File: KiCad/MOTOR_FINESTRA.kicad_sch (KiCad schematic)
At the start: 0 parts

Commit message: Actulització del driver del motor de finestra
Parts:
- added C10: 10uF, symbol Device:C
- added C11, C12, C9: 100nF, symbol Device:C
- added U3: VNH5019A-E, Package_SO:ST_MultiPowerSO-30, symbol Driver_Motor:VNH5019A-E
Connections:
- new net: C12.2, U3.11 (CP)
- new net GND: C10.2, C11.2, C12.1, C9.2, U3.6 (CS_DIS)
- new net GND_PWR: U3.18 (GNDB), U3.19 (GNDB), U3.20 (GNDB), U3.26 (GNDA), U3.27 (GNDA), U3.28 (GNDA)
- new net VBAT_PROT: C10.1, C9.1, U3.12 (VBAT)
- new net VDD_3V3: C11.1, U3.13 (VCC), U3.23 (VCC), U3.3 (VCC), U3.31 (VCC)
- new net WIN_CURRENT_ADC: U3.8 (CS)
- new net WIN_DIAGA: U3.5 (EN/DIAGA)
- new net WIN_DIAGB: U3.9 (EN/DIAGB)
- new net WIN_INA: U3.4 (INA)
- new net WIN_INB: U3.10 (INB)
- new net WIN_MOTOR_A: U3.1 (OUTA), U3.25 (OUTA), U3.30 (OUTA), U3.33 (OUTA)
- new net WIN_MOTOR_B: U3.15 (OUTB), U3.16 (OUTB), U3.21 (OUTB), U3.32 (OUTB)
- new net WIN_PWM: U3.7 (PWM)

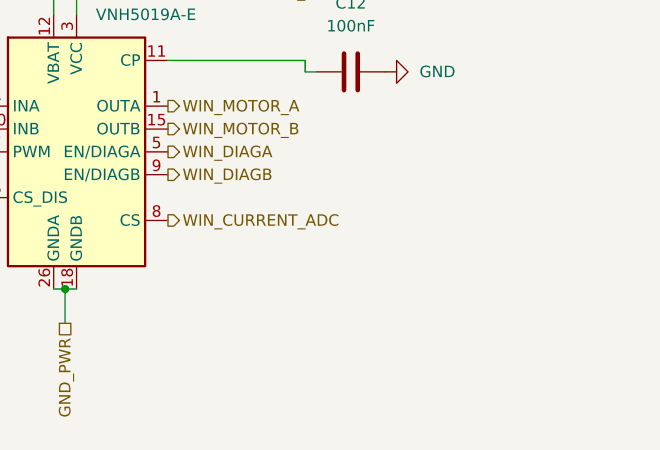
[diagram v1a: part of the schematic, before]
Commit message: Esquematic general conectat
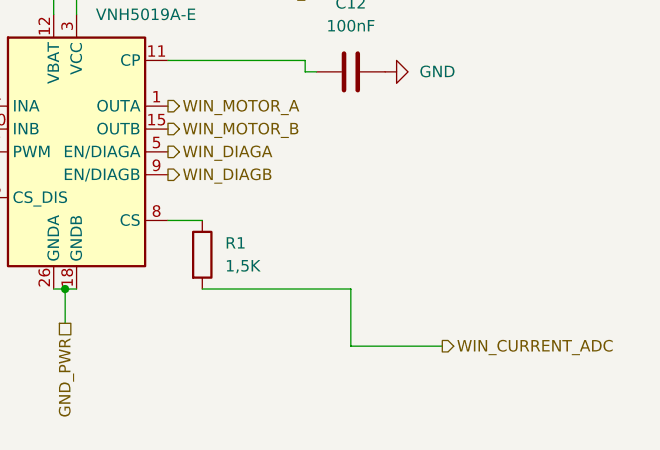
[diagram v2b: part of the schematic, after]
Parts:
- added R1: 1,5K, symbol Device:R
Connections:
- net WIN_CURRENT_ADC: now also R1.2; no longer U3.8 (CS)
- new net: R1.1, U3.8 (CS)
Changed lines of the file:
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@@
+	(wire
+		(pts
+			(xy 162.56 106.68) (xy 146.05 106.68)
+		)
+		(stroke
+			(width 0)
+			(type default)
+		)
+	)
+	(wire
+		(pts
+			(xy 162.56 106.68) (xy 162.56 113.03)
+		)
+		(stroke
+			(width 0)
+			(type default)
+		)
+	)
+	(wire
+		(pts
+			(xy 162.56 113.03) (xy 172.72 113.03)
+		)
+		(stroke
+			(width 0)
+			(type default)
+		)
+	)
+	(wire
+		(pts
+			(xy 142.24 99.06) (xy 146.05 99.06)
+		)
+		(stroke
+			(width 0)
+			(type default)
+		)
+	)
 	(wire
 		(pts
@@
 	(hierarchical_label "WIN_CURRENT_ADC"
 		(shape output)
-		(at 142.24 99.06 0)
+		(at 172.72 113.03 0)
 		(effects
 			(font
@@
 					(unit 1)
 				)
+			)
+		)
+	)
+	(symbol
+		(lib_id "Device:R")
+		(at 146.05 102.87 0)
+		(unit 1)
+		(exclude_from_sim no)
+		(in_bom yes)
+		(on_board yes)
+		(dnp no)
+		(fields_autoplaced yes)
+		(property "Reference" "R1"
+			(at 148.59 101.5999 0)
+			(effects
+				(font
+					(size 1.27 1.27)
+				)
+				(justify left)
+			)
+		)
+		(property "Value" "1,5K"
+			(at 148.59 104.1399 0)
+			(effects
+				(font
+					(size 1.27 1.27)
+				)
+				(justify left)
+			)
+		)
+		(property "Footprint" ""
+			(at 144.272 102.87 90)
+			(effects
+				(font
+					(size 1.27 1.27)
+				)
+				(hide yes)
+			)
+		)
+		(property "Datasheet" "~"
+			(at 146.05 102.87 0)
+			(effects
+				(font
+					(size 1.27 1.27)
+				)
+				(hide yes)
+			)
+		)
+		(property "Description" "Resistor"
+			(at 146.05 102.87 0)
+			(effects
+				(font
+					(size 1.27 1.27)
+				)
+				(hide yes)
+			)
+		)
+		(pin "2"
+		)
+		(pin "1"
+		)
+		(instances
+			(project ""
+				(path "/347831db-5db9-4aff-ad32-e56fd770e219/b6effc59-48f1-49a7-95ce-6407716902cc"
+					(reference "R1")
+					(unit 1)
+				)

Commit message: ESQUEMATIC FINAL V.1
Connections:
- net GND: now also R1.2
- net WIN_CURRENT_ADC: now also R1.1, U3.8 (CS); no longer R1.2
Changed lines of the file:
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@@
 	(paper "A4")
+	(junction
+		(at 146.05 99.06)
+		(diameter 0)
+		(color 0 0 0 0)
+	)
 	(junction
 		(at 129.54 69.85)
@@
 	(wire
 		(pts
-			(xy 162.56 106.68) (xy 146.05 106.68)
-		)
-		(stroke
-			(width 0)
-			(type default)
-		)
-	)
-	(wire
-		(pts
-			(xy 162.56 106.68) (xy 162.56 113.03)
-		)
-		(stroke
-			(width 0)
-			(type default)
-		)
-	)
-	(wire
-		(pts
-			(xy 162.56 113.03) (xy 172.72 113.03)
+			(xy 149.86 99.06) (xy 146.05 99.06)
 		)
 		(stroke
@@
 	(hierarchical_label "WIN_CURRENT_ADC"
 		(shape output)
-		(at 172.72 113.03 0)
+		(at 149.86 99.06 0)
 		(effects
 			(font
@@
 					(unit 1)
 				)
+			)
+		)
+	)
+	(symbol
+		(lib_id "power:GND")
+		(at 146.05 106.68 0)
+		(unit 1)
+		(exclude_from_sim no)
+		(in_bom yes)
+		(on_board yes)
+		(dnp no)
+		(fields_autoplaced yes)
+		(property "Reference" "#PWR08"
+			(at 146.05 113.03 0)
+			(effects
+				(font
+					(size 1.27 1.27)
+				)
+				(hide yes)
+			)
+		)
+		(property "Value" "GND"
+			(at 146.05 111.76 0)
+			(effects
+				(font
+					(size 1.27 1.27)
+				)
+			)
+		)
+		(property "Footprint" ""
+			(at 146.05 106.68 0)
+			(effects
+				(font
+					(size 1.27 1.27)
+				)
+				(hide yes)
+			)
+		)
+		(property "Datasheet" ""
+			(at 146.05 106.68 0)
+			(effects
+				(font
+					(size 1.27 1.27)
+				)
+				(hide yes)
+			)
+		)
+		(property "Description" "Power symbol creates a global label with name \"GND\" , ground"
+			(at 146.05 106.68 0)
+			(effects
+				(font
+					(size 1.27 1.27)
+				)
+				(hide yes)
+			)
+		)
+		(pin "1"
+		)
+		(instances
+			(project "PROJECTE_EINES"
+				(path "/347831db-5db9-4aff-ad32-e56fd770e219/b6effc59-48f1-49a7-95ce-6407716902cc"
+					(reference "#PWR08")
+					(unit 1)
+				)

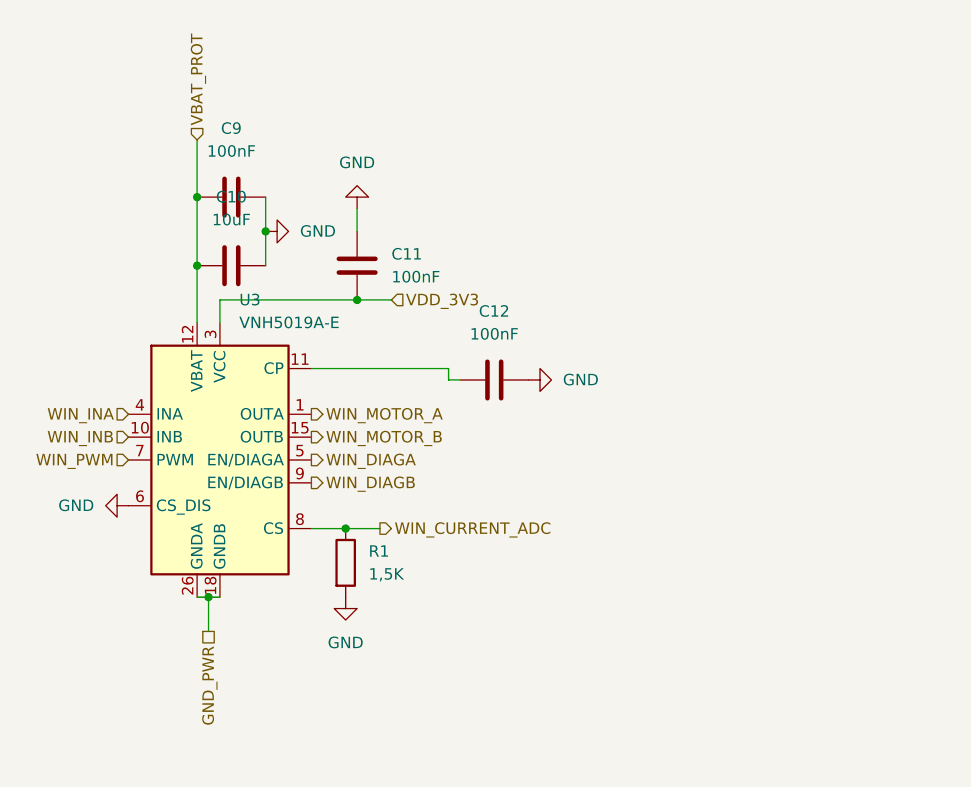
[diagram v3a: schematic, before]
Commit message: Nova versió diagrama de blocs + BOM actualitzat + Nova versió KiCad
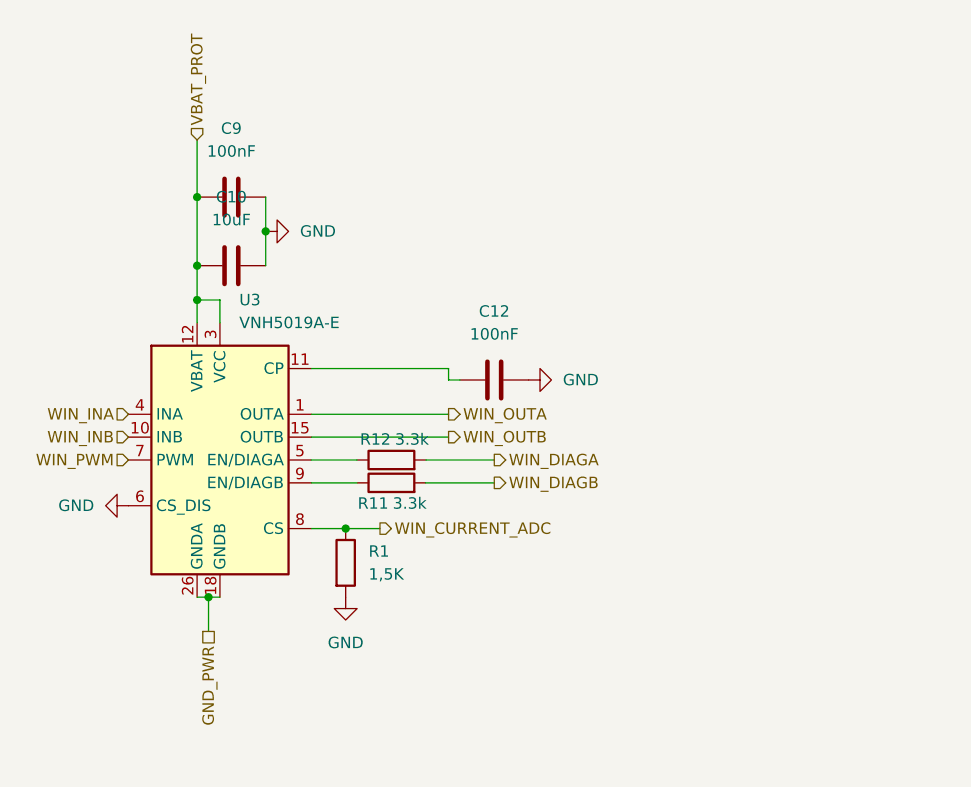
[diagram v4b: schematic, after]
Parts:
- removed C11: 100nF, symbol Device:C
- added R11, R12: 3.3k, Resistor_SMD:R_0805_2012Metric_Pad1.20x1.40mm_HandSolder, symbol Device:R
- R1: footprint (none) -> Resistor_SMD:R_0805_2012Metric_Pad1.20x1.40mm_HandSolder
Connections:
- net VDD_3V3 is gone; now on net VBAT_PROT: U3.13 (VCC), U3.23 (VCC), U3.3 (VCC), U3.31 (VCC)
- net WIN_DIAGA: now also R12.2; no longer U3.5 (EN/DIAGA)
- net WIN_DIAGB: now also R11.2; no longer U3.9 (EN/DIAGB)
- net WIN_MOTOR_A renamed WIN_OUTA
- net WIN_MOTOR_B renamed WIN_OUTB
- new net: R12.1, U3.5 (EN/DIAGA)
- new net: R11.1, U3.9 (EN/DIAGB)

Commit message: Resistències pull-up arreglades als motors
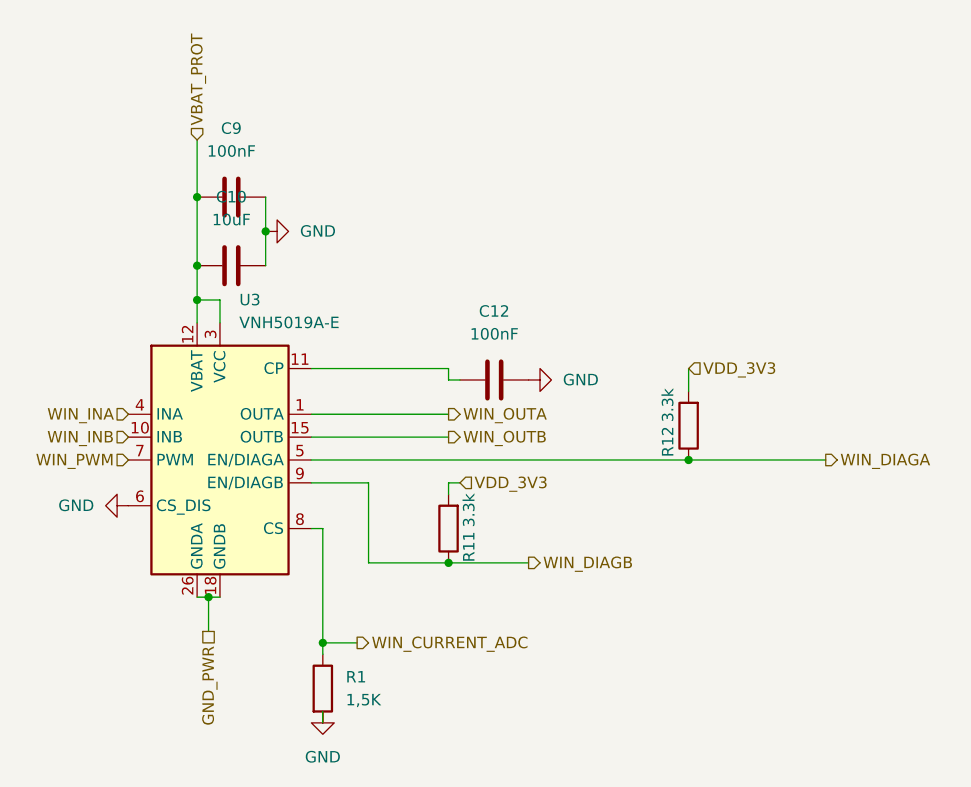
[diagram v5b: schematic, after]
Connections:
- net WIN_DIAGA: now also R12.1, U3.5 (EN/DIAGA); no longer R12.2
- net WIN_DIAGB: now also R11.1, U3.9 (EN/DIAGB); no longer R11.2
- new net VDD_3V3: R11.2, R12.2
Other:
- moved on the sheet: R1, R11, R12
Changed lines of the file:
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@@
 	)
 	(junction
-		(at 146.05 99.06)
+		(at 157.48 102.87)
+		(diameter 0)
+		(color 0 0 0 0)
+	)
+	(junction
+		(at 143.51 111.76)
 		(diameter 0)
 		(color 0 0 0 0)
@@
 	)
 	(junction
+		(at 184.15 91.44)
+		(diameter 0)
+		(color 0 0 0 0)
+	)
+	(junction
 		(at 129.54 62.23)
 		(diameter 0)
@@
 	(wire
 		(pts
-			(xy 147.32 93.98) (xy 142.24 93.98)
-		)
-		(stroke
-			(width 0)
-			(type default)
-		)
-	)
-	(wire
-		(pts
-			(xy 147.32 91.44) (xy 142.24 91.44)
-		)
-		(stroke
-			(width 0)
-			(type default)
-		)
-	)
-	(wire
-		(pts
-			(xy 162.56 93.98) (xy 154.94 93.98)
+			(xy 148.59 102.87) (xy 157.48 102.87)
+		)
+		(stroke
+			(width 0)
+			(type default)
+		)
+	)
+	(wire
+		(pts
+			(xy 142.24 91.44) (xy 184.15 91.44)
+		)
+		(stroke
+			(width 0)
+			(type default)
+		)
+	)
+	(wire
+		(pts
+			(xy 158.75 93.98) (xy 157.48 93.98)
 		)
 		(stroke
@@
 	(wire
 		(pts
+			(xy 148.59 102.87) (xy 148.59 93.98)
+		)
+		(stroke
+			(width 0)
+			(type default)
+		)
+	)
+	(wire
+		(pts
 			(xy 130.81 106.68) (xy 130.81 110.49)
 		)
@@
 	(wire
 		(pts
-			(xy 149.86 99.06) (xy 146.05 99.06)
-		)
-		(stroke
-			(width 0)
-			(type default)
-		)
-	)
-	(wire
-		(pts
-			(xy 142.24 99.06) (xy 146.05 99.06)
+			(xy 147.32 111.76) (xy 143.51 111.76)
 		)
 		(stroke
@@
 	(wire
 		(pts
+			(xy 148.59 93.98) (xy 142.24 93.98)
+		)
+		(stroke
+			(width 0)
+			(type default)
+		)
+	)
+	(wire
+		(pts
 			(xy 129.54 73.66) (xy 132.08 73.66)
 		)
@@
 	(wire
 		(pts
+			(xy 157.48 93.98) (xy 157.48 95.25)
+		)
+		(stroke
+			(width 0)
+			(type default)
+		)
+	)
+	(wire
+		(pts
 			(xy 129.54 69.85) (xy 129.54 73.66)
 		)
@@
 	(wire
 		(pts
+			(xy 143.51 111.76) (xy 143.51 99.06)
+		)
+		(stroke
+			(width 0)
+			(type default)
+		)
+	)
+	(wire
+		(pts
+			(xy 184.15 81.28) (xy 184.15 83.82)
+		)
+		(stroke
+			(width 0)
+			(type default)
+		)
+	)
+	(wire
+		(pts
 			(xy 157.48 82.55) (xy 158.75 82.55)
 		)
@@
 	(wire
 		(pts
-			(xy 162.56 91.44) (xy 154.94 91.44)
-		)
-		(stroke
-			(width 0)
-			(type default)
-		)
-	)
-	(wire
-		(pts
 			(xy 129.54 62.23) (xy 129.54 69.85)
 		)
@@
 	(wire
 		(pts
+			(xy 157.48 102.87) (xy 166.37 102.87)
+		)
+		(stroke
+			(width 0)
+			(type default)
+		)
+	)
+	(wire
+		(pts
 			(xy 142.24 86.36) (xy 157.48 86.36)
 		)
@@
 	(wire
 		(pts
+			(xy 143.51 120.65) (xy 143.51 119.38)
+		)
+		(stroke
+			(width 0)
+			(type default)
+		)
+	)
+	(wire
+		(pts
 			(xy 157.48 81.28) (xy 142.24 81.28)
 		)
@@
 			(width 0)
 			(type default)
+		)
+	)
+	(wire
+		(pts
+			(xy 143.51 99.06) (xy 142.24 99.06)
+		)
+		(stroke
+			(width 0)
+			(type default)
+		)
+	)
+	(wire
+		(pts
+			(xy 184.15 91.44) (xy 199.39 91.44)
+		)
+		(stroke
+			(width 0)
+			(type default)
+		)
+	)
+	(wire
+		(pts
+			(xy 143.51 113.03) (xy 143.51 111.76)
+		)
+		(stroke
+			(width 0)
+			(type default)
+		)
+	)
+	(hierarchical_label "VDD_3V3"
+		(shape input)
+		(at 158.75 93.98 0)
+		(effects
+			(font
+				(size 1.27 1.27)
+			)
+			(justify left)
+		)
+	)
+	(hierarchical_label "VDD_3V3"
+		(shape input)
+		(at 184.15 81.28 0)
+		(effects
+			(font
+				(size 1.27 1.27)
+			)
+			(justify left)
 		)
 	)
@@
 	(hierarchical_label "WIN_DIAGA"
 		(shape output)
-		(at 162.56 91.44 0)
+		(at 199.39 91.44 0)
 		(effects
 			(font
@@
 	(hierarchical_label "WIN_CURRENT_ADC"
 		(shape output)
-		(at 149.86 99.06 0)
+		(at 147.32 111.76 0)
 		(effects
 			(font
@@
 	(hierarchical_label "WIN_DIAGB"
 		(shape output)
-		(at 162.56 93.98 0)
+		(at 166.37 102.87 0)
 		(effects
 			(font
@@
 	(symbol
 		(lib_id "Device:R")
-		(at 151.13 91.44 90)
+		(at 184.15 87.63 180)
 		(unit 1)
 		(exclude_from_sim no)
@@
 		(dnp no)
 		(property "Reference" "R12"
-			(at 149.352 89.154 90)
+			(at 181.864 89.408 90)
 			(effects
 				(font
@@
 		)
 		(property "Value" "3.3k"
-			(at 153.416 89.154 90)
+			(at 181.864 85.344 90)
 			(effects
 				(font
@@
 		)
 		(property "Footprint" "Resistor_SMD:R_0805_2012Metric_Pad1.20x1.40mm_HandSolder"
-			(at 151.13 93.218 90)
+			(at 185.928 87.63 90)
 			(effects
 				(font
@@
 		)
 		(property "Datasheet" "~"
-			(at 151.13 91.44 0)
+			(at 184.15 87.63 0)
 			(effects
 				(font
@@
 		)
 		(property "Description" "Resistor"
-			(at 151.13 91.44 0)
+			(at 184.15 87.63 0)
 			(effects
 				(font
@@
 	(symbol
 		(lib_id "Device:R")
-		(at 151.13 93.98 90)
+		(at 157.48 99.06 180)
 		(unit 1)
 		(exclude_from_sim no)
@@
 		(dnp no)
 		(property "Reference" "R11"
-			(at 149.098 96.266 90)
+			(at 159.766 101.092 90)
 			(effects
 				(font
@@
 		)
 		(property "Value" "3.3k"
-			(at 153.162 96.266 90)
+			(at 159.766 97.028 90)
 			(effects
 				(font
@@
 		)
 		(property "Footprint" "Resistor_SMD:R_0805_2012Metric_Pad1.20x1.40mm_HandSolder"
-			(at 151.13 95.758 90)
+			(at 159.258 99.06 90)
 			(effects
 				(font
@@
 		)
 		(property "Datasheet" "~"
-			(at 151.13 93.98 0)
+			(at 157.48 99.06 0)
 			(effects
 				(font
@@
 		)
 		(property "Description" "Resistor"
-			(at 151.13 93.98 0)
+			(at 157.48 99.06 0)
 			(effects
 				(font
@@
 	(symbol
 		(lib_id "power:GND")
-		(at 146.05 106.68 0)
+		(at 143.51 119.38 0)
 		(unit 1)
 		(exclude_from_sim no)
@@
 		(fields_autoplaced yes)
 		(property "Reference" "#PWR08"
-			(at 146.05 113.03 0)
+			(at 143.51 125.73 0)
 			(effects
 				(font
@@
 		)
 		(property "Value" "GND"
-			(at 146.05 111.76 0)
+			(at 143.51 124.46 0)
 			(effects
 				(font
@@
 		)
 		(property "Footprint" ""
-			(at 146.05 106.68 0)
+			(at 143.51 119.38 0)
 			(effects
 				(font
@@
 		)
 		(property "Datasheet" ""
-			(at 146.05 106.68 0)
+			(at 143.51 119.38 0)
 			(effects
 				(font
@@
 		)
 		(property "Description" "Power symbol creates a global label with name \"GND\" , ground"
-			(at 146.05 106.68 0)
+			(at 143.51 119.38 0)
 			(effects
 				(font
@@
 	(symbol
 		(lib_id "Device:R")
-		(at 146.05 102.87 0)
+		(at 143.51 116.84 0)
 		(unit 1)
 		(exclude_from_sim no)
@@
 		(fields_autoplaced yes)
 		(property "Reference" "R1"
-			(at 148.59 101.5999 0)
+			(at 146.05 115.5699 0)
 			(effects
 				(font
@@
 		)
 		(property "Value" "1,5K"
-			(at 148.59 104.1399 0)
+			(at 146.05 118.1099 0)
 			(effects
 				(font
@@
 		)
 		(property "Footprint" "Resistor_SMD:R_0805_2012Metric_Pad1.20x1.40mm_HandSolder"
-			(at 144.272 102.87 90)
+			(at 141.732 116.84 90)
 			(effects
 				(font
@@
 		)
 		(property "Datasheet" "~"
-			(at 146.05 102.87 0)
+			(at 143.51 116.84 0)
 			(effects
 				(font
@@
 		)
 		(property "Description" "Resistor"
-			(at 146.05 102.87 0)
-			(effects
-				(font
+			(at 143.51 116.84 0)
+			(effects
+				(font

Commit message: Etiquetes de GND i VCC 3.3V canviades a simbols
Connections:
- net GND_PWR renamed GNDPWR
- net VDD_3V3 renamed +3.3V
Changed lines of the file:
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@@
-	(wire
-		(pts
-			(xy 158.75 93.98) (xy 157.48 93.98)
-		)
-		(stroke
-			(width 0)
-			(type default)
-		)
-	)
 	(wire
 		(pts
@@
 	(wire
 		(pts
-			(xy 157.48 93.98) (xy 157.48 95.25)
-		)
-		(stroke
-			(width 0)
-			(type default)
-		)
-	)
-	(wire
-		(pts
 			(xy 129.54 69.85) (xy 129.54 73.66)
 		)
@@
 			(width 0)
 			(type default)
-		)
-	)
-	(hierarchical_label "VDD_3V3"
-		(shape input)
-		(at 158.75 93.98 0)
-		(effects
-			(font
-				(size 1.27 1.27)
-			)
-			(justify left)
-		)
-	)
-	(hierarchical_label "VDD_3V3"
-		(shape input)
-		(at 184.15 81.28 0)
-		(effects
-			(font
-				(size 1.27 1.27)
-			)
-			(justify left)
 		)
 	)
@@
 		)
 	)
-	(hierarchical_label "GND_PWR"
-		(shape passive)
-		(at 130.81 110.49 270)
-		(effects
-			(font
-				(size 1.27 1.27)
-			)
-			(justify right)
-		)
-	)
 	(hierarchical_label "WIN_OUTB"
 		(shape output)
@@
 			)
 			(justify left)
+		)
+	)
+	(symbol
+		(lib_id "power:GNDPWR")
+		(at 130.81 110.49 0)
+		(unit 1)
+		(exclude_from_sim no)
+		(in_bom yes)
+		(on_board yes)
+		(dnp no)
+		(fields_autoplaced yes)
+		(property "Reference" "#PWR037"
+			(at 130.81 115.57 0)
+			(effects
+				(font
+					(size 1.27 1.27)
+				)
+				(hide yes)
+			)
+		)
+		(property "Value" "GNDPWR"
+			(at 130.683 114.3 0)
+			(effects
+				(font
+					(size 1.27 1.27)
+				)
+			)
+		)
+		(property "Footprint" ""
+			(at 130.81 111.76 0)
+			(effects
+				(font
+					(size 1.27 1.27)
+				)
+				(hide yes)
+			)
+		)
+		(property "Datasheet" ""
+			(at 130.81 111.76 0)
+			(effects
+				(font
+					(size 1.27 1.27)
+				)
+				(hide yes)
+			)
+		)
+		(property "Description" "Power symbol creates a global label with name \"GNDPWR\" , global ground"
+			(at 130.81 110.49 0)
+			(effects
+				(font
+					(size 1.27 1.27)
+				)
+				(hide yes)
+			)
+		)
+		(pin "1"
+		)
+		(instances
+			(project ""
+				(path "/347831db-5db9-4aff-ad32-e56fd770e219/b6effc59-48f1-49a7-95ce-6407716902cc"
+					(reference "#PWR037")
+					(unit 1)
+				)
+			)
 		)
 	)
@@
 				(path "/347831db-5db9-4aff-ad32-e56fd770e219/b6effc59-48f1-49a7-95ce-6407716902cc"
 					(reference "R12")
+					(unit 1)
+				)
+			)
+		)
+	)
+	(symbol
+		(lib_id "power:+3.3V")
+		(at 184.15 81.28 0)
+		(unit 1)
+		(exclude_from_sim no)
+		(in_bom yes)
+		(on_board yes)
+		(dnp no)
+		(property "Reference" "#PWR039"
+			(at 184.15 85.09 0)
+			(effects
+				(font
+					(size 1.27 1.27)
+				)
+				(hide yes)
+			)
+		)
+		(property "Value" "+3.3V"
+			(at 180.086 79.756 0)
+			(effects
+				(font
+					(size 1.27 1.27)
+				)
+			)
+		)
+		(property "Footprint" ""
+			(at 184.15 81.28 0)
+			(effects
+				(font
+					(size 1.27 1.27)
+				)
+				(hide yes)
+			)
+		)
+		(property "Datasheet" ""
+			(at 184.15 81.28 0)
+			(effects
+				(font
+					(size 1.27 1.27)
+				)
+				(hide yes)
+			)
+		)
+		(property "Description" "Power symbol creates a global label with name \"+3.3V\""
+			(at 184.15 81.28 0)
+			(effects
+				(font
+					(size 1.27 1.27)
+				)
+				(hide yes)
+			)
+		)
+		(pin "1"
+		)
+		(instances
+			(project "PROJECTE_EINES"
+				(path "/347831db-5db9-4aff-ad32-e56fd770e219/b6effc59-48f1-49a7-95ce-6407716902cc"
+					(reference "#PWR039")
 					(unit 1)
 				)
@@
 					(unit 1)
 				)
+			)
+		)
+	)
+	(symbol
+		(lib_id "power:+3.3V")
+		(at 157.48 95.25 0)
+		(unit 1)
+		(exclude_from_sim no)
+		(in_bom yes)
+		(on_board yes)
+		(dnp no)
+		(property "Reference" "#PWR038"
+			(at 157.48 99.06 0)
+			(effects
+				(font
+					(size 1.27 1.27)
+				)
+				(hide yes)
+			)
+		)
+		(property "Value" "+3.3V"
+			(at 153.416 93.726 0)
+			(effects
+				(font
+					(size 1.27 1.27)
+				)
+			)
+		)
+		(property "Footprint" ""
+			(at 157.48 95.25 0)
+			(effects
+				(font
+					(size 1.27 1.27)
+				)
+				(hide yes)
+			)
+		)
+		(property "Datasheet" ""
+			(at 157.48 95.25 0)
+			(effects
+				(font
+					(size 1.27 1.27)
+				)
+				(hide yes)
+			)
+		)
+		(property "Description" "Power symbol creates a global label with name \"+3.3V\""
+			(at 157.48 95.25 0)
+			(effects
+				(font
+					(size 1.27 1.27)
+				)
+				(hide yes)
+			)
+		)
+		(pin "1"
+		)
+		(instances
+			(project ""
+				(path "/347831db-5db9-4aff-ad32-e56fd770e219/b6effc59-48f1-49a7-95ce-6407716902cc"
+					(reference "#PWR038")
+					(unit 1)
+				)
